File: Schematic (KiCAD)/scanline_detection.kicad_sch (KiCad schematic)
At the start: 95 parts, among them M2 NOR_2, M3 BIGBUF, X12 D-FF Reset, X13 NAND_2, X14 BUFFER, X16 INVERT, X17 NAND_2, X26 INVERT, X27 D-FF No Reset, X28 INVERT, X4 NAND_2, X5 D-FF No Reset, X6 NAND_4, X7 INVERT, X8 Reg 2 DFF-No-Reset N, X9 NAND_2, Y1 BUFFER, Y10 XNOR_2, Y13 XNOR_2, Y15 NOR_2, Y17 XNOR_2, Y2,7,9,14,16,21,23,28 Reg 8 D-Latch, Y20 XNOR_2, Y22 NAND_4, Y24 XNOR_2, Y27 XNOR_2, Y29 NOR_2, Y3 XNOR_2, Y30 INVERT, Y31 D-FF Reset, Y32 INVERT, Y6 XNOR_2, Y8 NAND_4

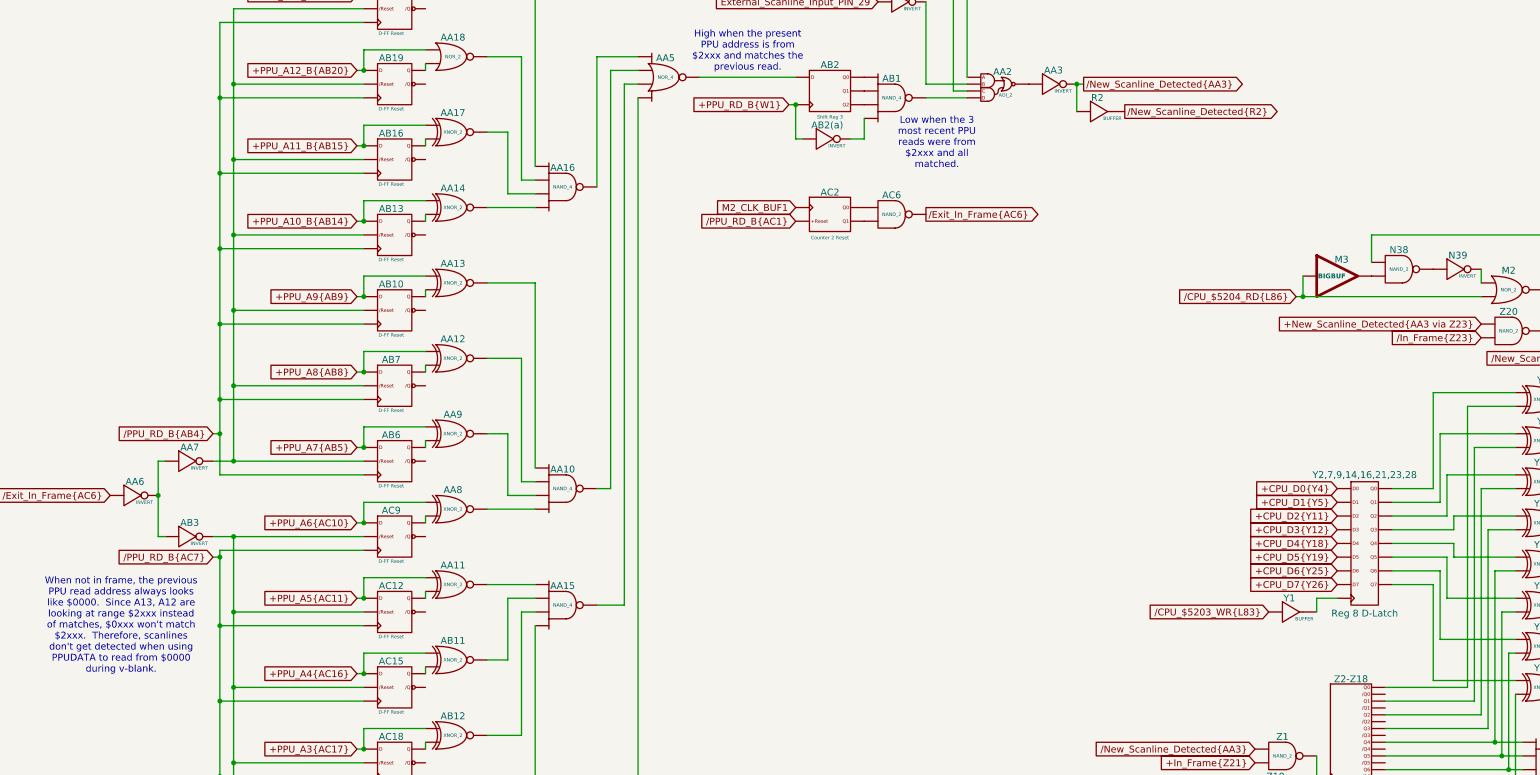
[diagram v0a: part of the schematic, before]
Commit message: - Started work on the pulse channels.  - Solved at least 2 of the red traces in the SVG.  - Finally realized that "Unknown 4to1" cells are actually just ordinary And-Or-Invert "AOI22" cells.
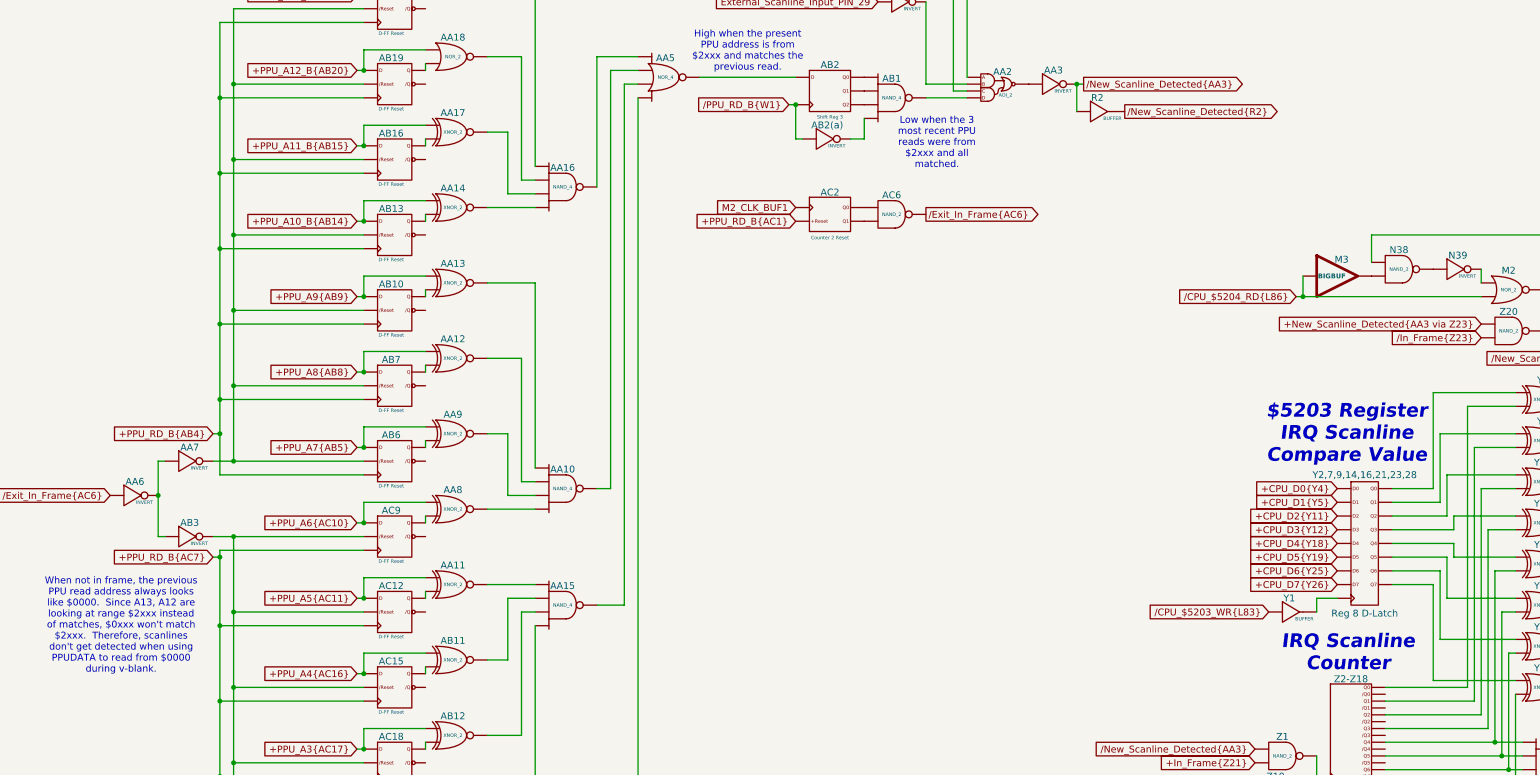
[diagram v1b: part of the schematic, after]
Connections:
- net +PPU_RD_B{W1} is gone; now on net /PPU_RD_B{W1}: AB2(a). (X), AB2. (Q2)
- net /PPU_RD_B{AB4} is gone; now on net +PPU_RD_B{AB4}: AB10. (/Q), AB13. (/Q), AB16. (/Q), AB19. (/Q), AB22. (/Q), AB6. (/Q), AB7. (/Q)
- net /PPU_RD_B{AC1} is gone; now on net M2_CLK_BUF1: AC2. (Q1)
- net /PPU_RD_B{AC7} is gone; now on net +PPU_RD_B{AC7}: AC12. (/Q), AC15. (/Q), AC18. (/Q), AC21. (/Q), AC24. (/Q), AC27. (/Q), AC9. (/Q)
- net at X7. (X): now also Z23. (/Q); no longer X6. (X)
- net at X13. (X): now also X12. (/Q); no longer X14. (X)
- net at X9. (X): now also Z24. (X); no longer X8. (/Q1)
- net +PPU_RD_B{AB4}: now reaches AB6. (/Q)
- net +PPU_RD_B{AB4}: no longer AA9. (X)
- net at AA10. (X): now also AA13. (X); no longer AA9. (X)
- net at AA16. (X): now also AA14. (X); no longer AA17. (X)
- net at Z2-Z18. (/Q7): now also Y3. (X); no longer Z19. (X)
- net at Y29. (X): now also Y31. (/Q); no longer Y30. (X)
- net at Y15. (X): now also Y22. (X); no longer Y29. (X)
- net at Y17. (X): now also Y22. (X); no longer Y2,7,9,14,16,21,23,28. (Q7)
- net at Y24. (X): now also Y22. (X); no longer Y2,7,9,14,16,21,23,28. (Q7)
- net at Y20. (X): now also Y22. (X); no longer Y2,7,9,14,16,21,23,28. (Q7)
- net at Y6. (X): now also Y8. (X); no longer Y2,7,9,14,16,21,23,28. (Q7)
- net at Y13. (X): now also Y8. (X); no longer Y2,7,9,14,16,21,23,28. (Q7)
- net at Y10. (X): now also Y8. (X); no longer Y2,7,9,14,16,21,23,28. (Q7)
- net at Y3. (X): now also Y8. (X); no longer Y2,7,9,14,16,21,23,28. (Q7)
- net at Y27. (X): now also Y22. (X); no longer Y2,7,9,14,16,21,23,28. (Q7)
- net at AA20. (X): now also AA16. (X); no longer AA21. (X)
- net +PPU_RD_B{AC7}: now reaches AC15. (/Q)
- net at AA19. (X): now also AB18. (X); no longer AA22. (X)
- net at AA15. (X): now also AB17. (X); no longer AA11. (X)
- net at X17. (X): now also Z20. (X); no longer X26. (X)
- net at Y8. (X): now also Y15. (X); no longer Y6. (X)
- net at AA5. (X): now also AA15. (X); no longer AA10. (X)
- net /PPU_RD_B{W1}: now reaches AB2. (Q2)
- net /PPU_RD_B{W1}: no longer AA5. (X)
- net at AB1. (X): now also AB2(a). (X); no longer AA2. (X)
- net at N39. (X): now also N38. (X); no longer M2. (X)
- new net: X4. (X), X5. (/Q)
- new net: X16. (X), X4. (X)
- new net: X5. (/Q), X6. (X)
- new net: X6. (X), X7. (X)
- new net: X13. (X), X14. (X)
- new net: X13. (X), Y31. (/Q), Y32. (X)
- new net: X8. (/Q1), X9. (X) (x2)
- new net: AA9. (X), AB6. (/Q)
- new net: AA10. (X), AA9. (X)
- new net: AA17. (X), AB16. (/Q)
- new net: AA16. (X), AA17. (X)
- new net: Z19. (X), Z2-Z18. (/Q7)
- new net: Y29. (X), Y30. (X)
- new net: Y15. (X), Y29. (X)
- new net: Y1. (X), Y2,7,9,14,16,21,23,28. (Q7)
- new net: Y17. (X), Y2,7,9,14,16,21,23,28. (Q7)
- new net: Y2,7,9,14,16,21,23,28. (Q7), Y24. (X)
- new net: Y2,7,9,14,16,21,23,28. (Q7), Y20. (X)
- new net: Y2,7,9,14,16,21,23,28. (Q7), Y6. (X)
- new net: Y13. (X), Y2,7,9,14,16,21,23,28. (Q7)
- new net: Y10. (X), Y2,7,9,14,16,21,23,28. (Q7)
- new net: Y2,7,9,14,16,21,23,28. (Q7), Y3. (X)
- new net: Y2,7,9,14,16,21,23,28. (Q7), Y27. (X)
- new net: AA20. (X), AA21. (X)
- new net: AA21. (X), AB22. (/Q)
- new net: AA7. (X), AB10. (/Q), AB13. (/Q), AB16. (/Q), AB19. (/Q), AB22. (/Q), AB6. (/Q), AB7. (/Q)
- new net: AB3. (X), AC12. (/Q), AC15. (/Q), AC18. (/Q), AC21. (/Q), AC24. (/Q), AC27. (/Q), AC9. (/Q)
- new net: AB11. (X), AC15. (/Q)
- new net: AA12. (X), AB7. (/Q)
- new net: Y17. (X), Z2-Z18. (/Q7), Z22. (X)
- new net: Y24. (X), Z2-Z18. (/Q7), Z22. (X)
- new net: Y20. (X), Z2-Z18. (/Q7), Z22. (X)
- new net: Y27. (X), Z2-Z18. (/Q7), Z22. (X)
- new net: Y6. (X), Z2-Z18. (/Q7)
- new net: Y13. (X), Z2-Z18. (/Q7)
- new net: Y10. (X), Z2-Z18. (/Q7)
- new net: Z1. (X), Z2-Z18. (/Q7)
- new net: AA10. (X), AA12. (X)
- new net: AA22. (X), AC27. (/Q)
- new net: AA11. (X), AC12. (/Q)
- new net: AC2. (Q1), AC6. (X) (x2)
- new net: AA19. (X), AA22. (X)
- new net: AA11. (X), AA15. (X)
- new net: AA18. (X), AB19. (/Q)
- new net: AA16. (X), AA18. (X)
- new net: X17. (X), X26. (X)
- new net: M2. (X), X17. (X)
- new net: AA10. (X), AA5. (X)
- new net: AA5. (X), AB2. (Q2)
- new net: AA19. (X), AA5. (X)
- new net: AA16. (X), AA5. (X)
- new net: AA10. (X), AA8. (X)
- new net: AA2. (X), AA3. (X)
- new net: AA2. (X), AA4. (X)
- new net: AA2. (X), AB1. (X)
- new net: Z24. (X), Z25. (X)
- new net: AA8. (X), AC9. (/Q)
- new net: M3. (X), N38. (X)
- new net: AB1. (X), AB2. (Q2) (x3)
- new net: M2. (X), N39. (X)
- new net: AA13. (X), AB10. (/Q)
- new net: AB17. (X), AC21. (/Q)
- new net: N16. (X), N9. (X)
- new net: AA15. (X), AB12. (X)
- new net: AB12. (X), AC18. (/Q)
- new net: X27. (/Q), X28. (X)
- new net: AB18. (X), AC24. (/Q)
- new net: AA14. (X), AB13. (/Q)
- new net: AA15. (X), AB11. (X)
- new net +PPU_RD_B{AC1}: AC2. (Q1)
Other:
- note added: "$5203 Register IRQ Scanline Compare Value"
- note added: "IRQ Scanline Counter"
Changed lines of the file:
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@@
 		)
 	)
+	(text "IRQ Scanline\nCounter"
+		(exclude_from_sim no)
+		(at 264.922 147.32 0)
+		(effects
+			(font
+				(size 2.54 2.54)
+				(thickness 0.508)
+				(bold yes)
+				(italic yes)
+			)
+		)
+	)
+	(text "$5203 Register\nIRQ Scanline\nCompare Value"
+		(exclude_from_sim no)
+		(at 264.668 106.68 0)
+		(effects
+			(font
+				(size 2.54 2.54)
+				(thickness 0.508)
+				(bold yes)
+				(italic yes)
+			)
+		)
+	)
 	(text "Hi when $5203\nmatches the present\nV-Split scanline.\n\nD'Morgan tells us\nthat we can pretend\nY8,Y15,Y22 are all\nAND gates."
 		(exclude_from_sim no)
@@
 		)
 	)
-	(global_label "{slash}PPU_RD_B{AC7}"
+	(global_label "+PPU_RD_B{AC7}"
 		(shape input)
 		(at 54.61 129.54 180)
@@
 		)
 		(property "Intersheetrefs" "${INTERSHEET_REFS}"
-			(at 35.4171 129.54 0)
+			(at 35.1752 129.54 0)
 			(effects
 				(font
@@
 		)
 	)
-	(global_label "{slash}PPU_RD_B{AC1}"
+	(global_label "+PPU_RD_B{AC1}"
 		(shape input)
 		(at 162.56 67.31 180)
@@
 		)
 		(property "Intersheetrefs" "${INTERSHEET_REFS}"
-			(at 143.3671 67.31 0)
+			(at 143.1252 67.31 0)
 			(effects
 				(font
@@
 		)
 	)
-	(global_label "+PPU_RD_B{W1}"
+	(global_label "{slash}PPU_RD_B{W1}"
 		(shape input)
 		(at 161.29 45.72 180)
@@
 		)
 		(property "Intersheetrefs" "${INTERSHEET_REFS}"
-			(at 142.7624 45.72 0)
+			(at 143.0043 45.72 0)
 			(effects
 				(font
@@
 		)
 	)
-	(global_label "{slash}PPU_RD_B{AB4}"
+	(global_label "+PPU_RD_B{AB4}"
 		(shape input)
 		(at 54.61 106.68 180)
@@
 		)
 		(property "Intersheetrefs" "${INTERSHEET_REFS}"
-			(at 35.4171 106.68 0)
+			(at 35.1752 106.68 0)
 			(effects
 				(font

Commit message: - Pulse DAC logic is now complete.  - The 4-bit adders are verified correct using Excel.    - This revealed 1 tracing error and also 3 XNOR gates that are actually XOR in this case.  - Now including a PDF version of the schematic.
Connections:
- net at X7. (X): now also Z23. (/Q); no longer X6. (X)
- net at X13. (X): now also X12. (/Q); no longer X14. (X)
- net at X9. (X): now also Z24. (X); no longer X8. (/Q1)
- net at AA10. (X): now also AA13. (X); no longer AA9. (X)
- net at AA16. (X): now also AA14. (X); no longer AA17. (X)
- net at Z2-Z18. (/Q7): now also Y3. (X); no longer Z19. (X)
- net at Y29. (X): now also Y31. (/Q); no longer Y30. (X)
- net at Y15. (X): now also Y22. (X); no longer Y29. (X)
- net at Y17. (X): now also Y22. (X); no longer Y2,7,9,14,16,21,23,28. (Q7)
- net at Y24. (X): now also Y22. (X); no longer Y2,7,9,14,16,21,23,28. (Q7)
- net at Y20. (X): now also Y22. (X); no longer Y2,7,9,14,16,21,23,28. (Q7)
- net at Y6. (X): now also Y8. (X); no longer Y2,7,9,14,16,21,23,28. (Q7)
- net at Y13. (X): now also Y8. (X); no longer Y2,7,9,14,16,21,23,28. (Q7)
- net at Y10. (X): now also Y8. (X); no longer Y2,7,9,14,16,21,23,28. (Q7)
- net at Y3. (X): now also Y8. (X); no longer Y2,7,9,14,16,21,23,28. (Q7)
- net at Y27. (X): now also Y22. (X); no longer Y2,7,9,14,16,21,23,28. (Q7)
- net at AA20. (X): now also AA16. (X); no longer AA21. (X)
- net at AA19. (X): now also AB18. (X); no longer AA22. (X)
- net at AA15. (X): now also AB17. (X); no longer AA11. (X)
- net at X17. (X): now also Z20. (X); no longer X26. (X)
- net at Y8. (X): now also Y15. (X); no longer Y6. (X)
- net at AA5. (X): now also AA15. (X); no longer AA10. (X)
- net at AB1. (X): now also AB2(a). (X); no longer AA2. (X)
- net at N39. (X): now also N38. (X); no longer M2. (X)
- new net: X4. (X), X5. (/Q)
- new net: X16. (X), X4. (X)
- new net: X5. (/Q), X6. (X)
- new net: X6. (X), X7. (X)
- new net: X13. (X), X14. (X)
- new net: X13. (X), Y31. (/Q), Y32. (X)
- new net: X8. (/Q1), X9. (X) (x2)
- new net: AA9. (X), AB6. (/Q)
- new net: AA10. (X), AA9. (X)
- new net: AA17. (X), AB16. (/Q)
- new net: AA16. (X), AA17. (X)
- new net: Z19. (X), Z2-Z18. (/Q7)
- new net: Y29. (X), Y30. (X)
- new net: Y15. (X), Y29. (X)
- new net: Y1. (X), Y2,7,9,14,16,21,23,28. (Q7)
- new net: Y17. (X), Y2,7,9,14,16,21,23,28. (Q7)
- new net: Y2,7,9,14,16,21,23,28. (Q7), Y24. (X)
- new net: Y2,7,9,14,16,21,23,28. (Q7), Y20. (X)
- new net: Y2,7,9,14,16,21,23,28. (Q7), Y6. (X)
- new net: Y13. (X), Y2,7,9,14,16,21,23,28. (Q7)
- new net: Y10. (X), Y2,7,9,14,16,21,23,28. (Q7)
- new net: Y2,7,9,14,16,21,23,28. (Q7), Y3. (X)
- new net: Y2,7,9,14,16,21,23,28. (Q7), Y27. (X)
- new net: AA20. (X), AA21. (X)
- new net: AA21. (X), AB22. (/Q)
- new net: AA7. (X), AB10. (/Q), AB13. (/Q), AB16. (/Q), AB19. (/Q), AB22. (/Q), AB6. (/Q), AB7. (/Q)
- new net: AB3. (X), AC12. (/Q), AC15. (/Q), AC18. (/Q), AC21. (/Q), AC24. (/Q), AC27. (/Q), AC9. (/Q)
- new net: AB11. (X), AC15. (/Q)
- new net: AA12. (X), AB7. (/Q)
- new net: Y17. (X), Z2-Z18. (/Q7), Z22. (X)
- new net: Y24. (X), Z2-Z18. (/Q7), Z22. (X)
- new net: Y20. (X), Z2-Z18. (/Q7), Z22. (X)
- new net: Y27. (X), Z2-Z18. (/Q7), Z22. (X)
- new net: Y6. (X), Z2-Z18. (/Q7)
- new net: Y13. (X), Z2-Z18. (/Q7)
- new net: Y10. (X), Z2-Z18. (/Q7)
- new net: Z1. (X), Z2-Z18. (/Q7)
- new net: AA10. (X), AA12. (X)
- new net: AA22. (X), AC27. (/Q)
- new net: AA11. (X), AC12. (/Q)
- new net: AC2. (Q1), AC6. (X) (x2)
- new net: AA19. (X), AA22. (X)
- new net: AA11. (X), AA15. (X)
- new net: AA18. (X), AB19. (/Q)
- new net: AA16. (X), AA18. (X)
- new net: X17. (X), X26. (X)
- new net: M2. (X), X17. (X)
- new net: AA10. (X), AA5. (X)
- new net: AA5. (X), AB2. (Q2)
- new net: AA19. (X), AA5. (X)
- new net: AA16. (X), AA5. (X)
- new net: AA10. (X), AA8. (X)
- new net: AA2. (X), AA3. (X)
- new net: AA2. (X), AA4. (X)
- new net: AA2. (X), AB1. (X)
- new net: Z24. (X), Z25. (X)
- new net: AA8. (X), AC9. (/Q)
- new net: M3. (X), N38. (X)
- new net: AB1. (X), AB2. (Q2) (x3)
- new net: M2. (X), N39. (X)
- new net: AA13. (X), AB10. (/Q)
- new net: AB17. (X), AC21. (/Q)
- new net: N16. (X), N9. (X)
- new net: AA15. (X), AB12. (X)
- new net: AB12. (X), AC18. (/Q)
- new net: X27. (/Q), X28. (X)
- new net: AB18. (X), AC24. (/Q)
- new net: AA14. (X), AB13. (/Q)
- new net: AA15. (X), AB11. (X)
